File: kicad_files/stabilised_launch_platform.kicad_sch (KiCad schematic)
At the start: 37 parts, among them J1 Conn_01x03_Male, J2 Conn_01x03_Male, J3 Conn_01x06_Male, J4 USB_C_Receptacle_USB2.0, SW1 SW_Push, U1 MAX7375AXR805, U2 AP7370-33Y, U3 STM32L011F3Px, U4 FT201XS, U5 LIS3DH

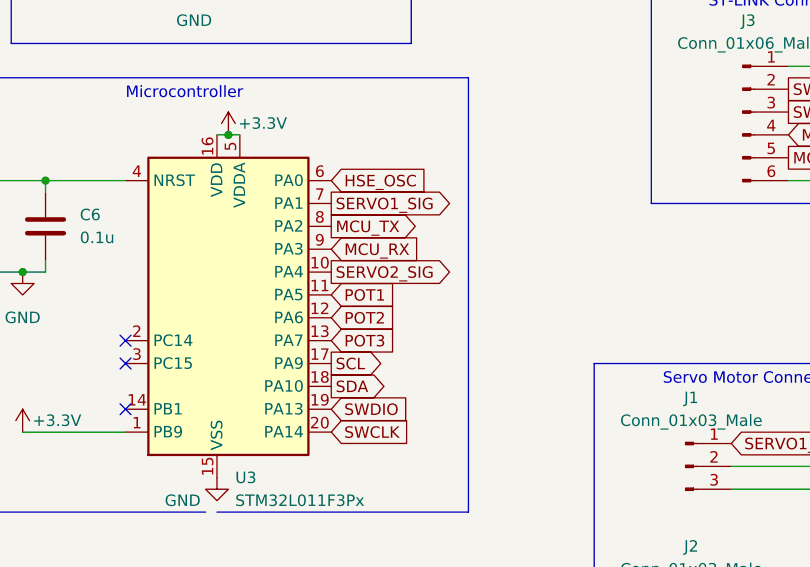
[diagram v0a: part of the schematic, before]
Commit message: fixed servo output
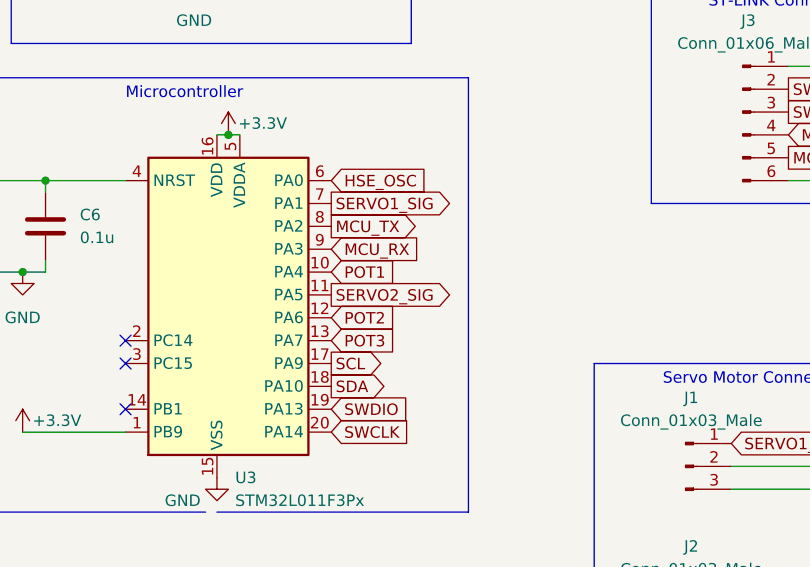
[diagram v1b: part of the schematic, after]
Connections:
- net POT1: now also U3.10 (PA4); no longer U3.11 (PA5)
- net SERVO2_SIG: now also U3.11 (PA5); no longer U3.10 (PA4)
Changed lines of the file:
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@@
     )
   )
-  (global_label "SERVO2_SIG" (shape output) (at 194.31 71.12 0) (fields_autoplaced)
+  (global_label "SERVO2_SIG" (shape output) (at 194.31 73.66 0) (fields_autoplaced)
     (effects (font (size 1.27 1.27)) (justify left))
-    (property "Intersheet References" "${INTERSHEET_REFS}" (id 0) (at 208.0321 71.0406 0)
+    (property "Intersheet References" "${INTERSHEET_REFS}" (id 0) (at 208.0321 73.5806 0)
       (effects (font (size 1.27 1.27)) (justify left) hide)
     )
@@
     )
   )
-  (global_label "POT1" (shape input) (at 194.31 73.66 0) (fields_autoplaced)
+  (global_label "POT1" (shape input) (at 194.31 71.12 0) (fields_autoplaced)
     (effects (font (size 1.27 1.27)) (justify left))
-    (property "Intersheet References" "${INTERSHEET_REFS}" (id 0) (at 201.5007 73.5806 0)
+    (property "Intersheet References" "${INTERSHEET_REFS}" (id 0) (at 201.5007 71.0406 0)
       (effects (font (size 1.27 1.27)) (justify left) hide)
     )

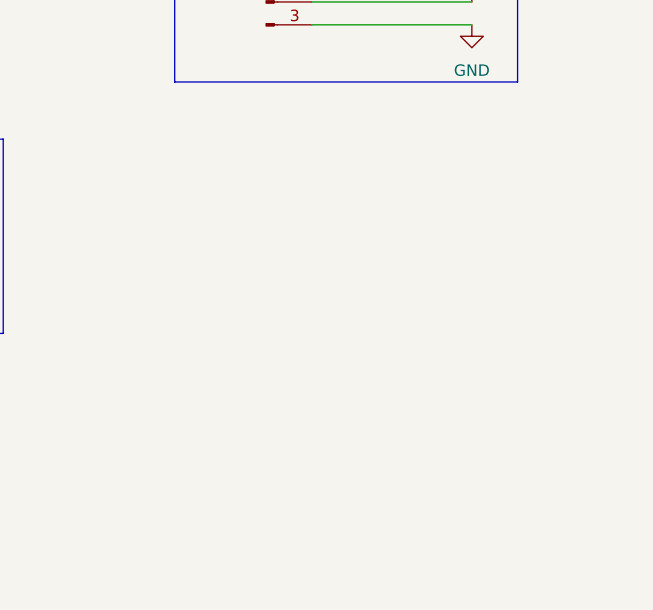
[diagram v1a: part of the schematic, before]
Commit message: fixed footprints, added mounting holes, fixed traces
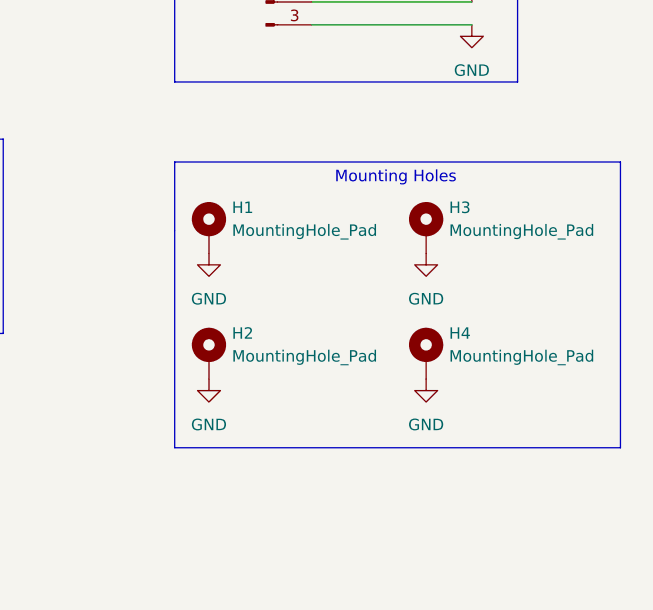
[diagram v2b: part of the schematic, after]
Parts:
- added H1, H2, H3, H4: MountingHole_Pad, MountingHole:MountingHole_3.2mm_M3_Pad, symbol Mechanical:MountingHole_Pad
- C14: footprint Capacitor_SMD:C_0805_2012Metric_Pad1.18x1.45mm_HandSolder -> Capacitor_THT:CP_Radial_D5.0mm_P2.00mm
- J1, J2: footprint Connector_PinHeader_1.00mm:PinHeader_1x03_P1.00mm_Vertical -> Connector_PinHeader_2.54mm:PinHeader_1x03_P2.54mm_Vertical
- J3: footprint Connector_PinHeader_1.00mm:PinHeader_1x06_P1.00mm_Vertical -> Connector_PinHeader_2.54mm:PinHeader_1x06_P2.54mm_Vertical
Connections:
- net GND: now also H1.1, H2.1, H3.1, H4.1
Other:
- note added: "Mounting Holes"
